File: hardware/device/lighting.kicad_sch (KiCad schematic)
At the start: 17 parts, among them U10 TRIG9, U11 TRIG13, U12 TRIG10, U13 TRIG14, U14 TRIG11, U15 TRIG15, U16 TRIG12, U17 TRIG16, U2 TRIG1, U3 TRIG2, U4 TRIG3, U5 TRIG4, U6 TRIG8, U7 TRIG7, U8 TRIG6, U9 TRIG5

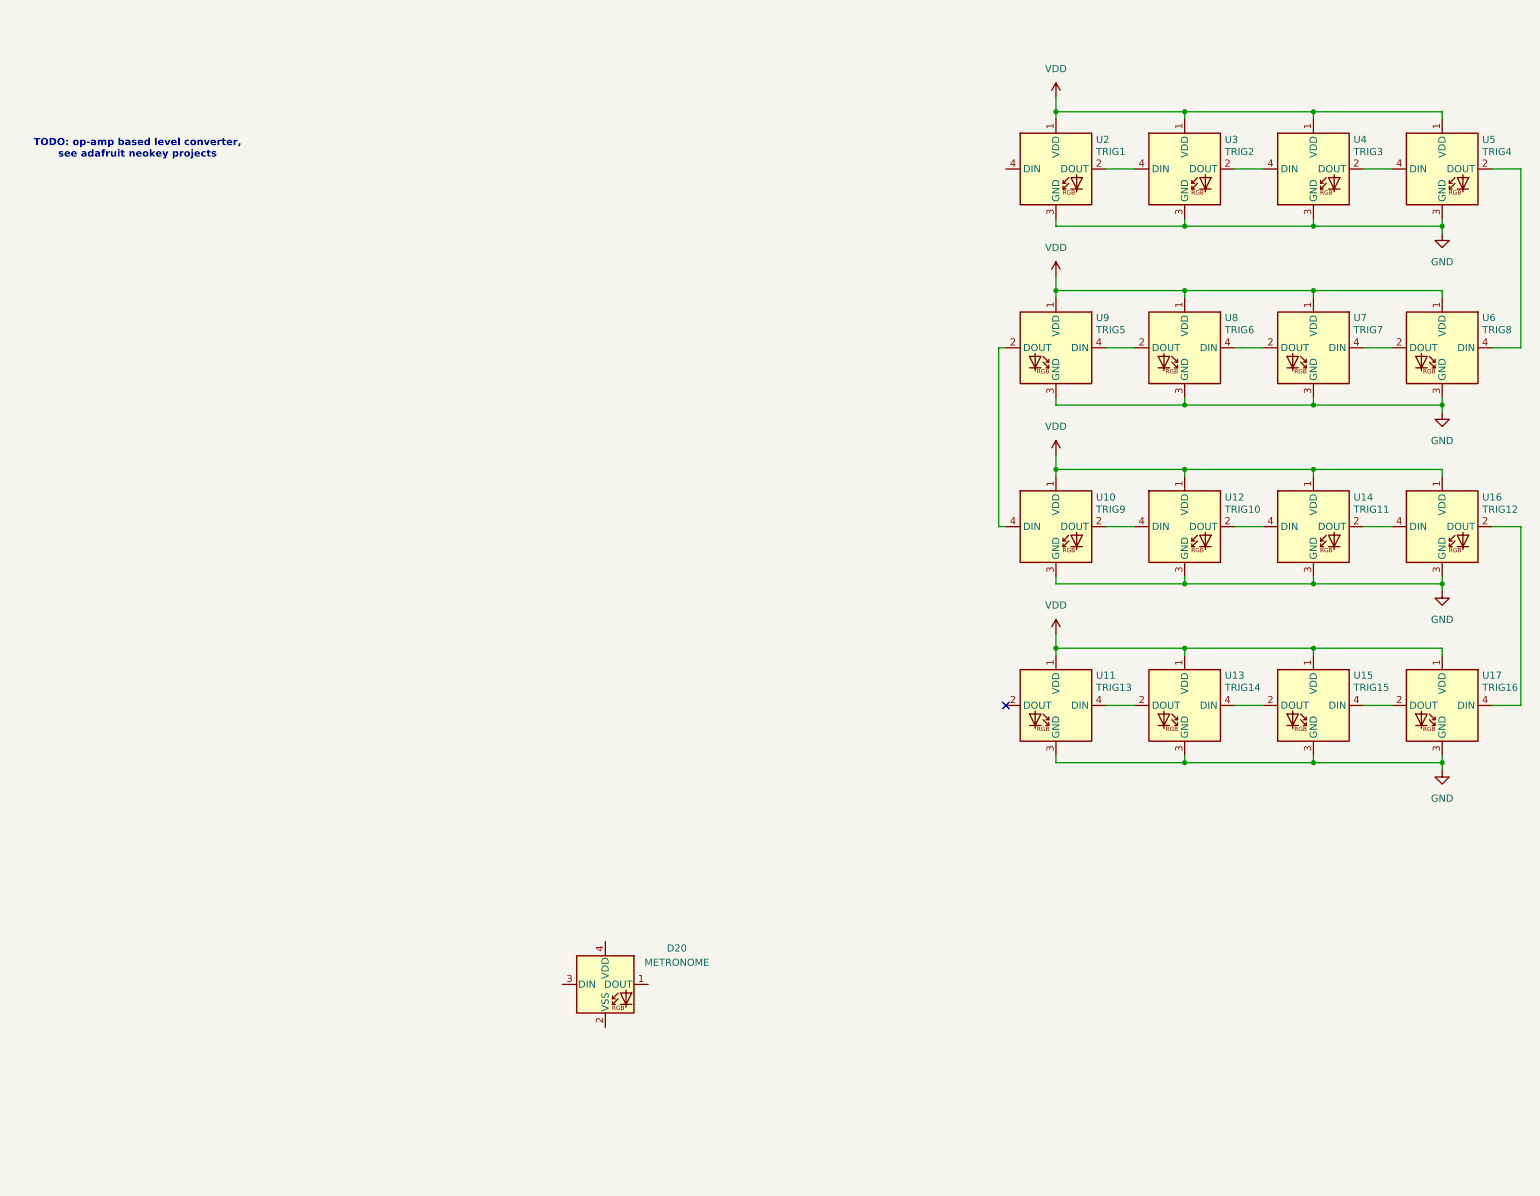
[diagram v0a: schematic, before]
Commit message: feat: add buffer for LED logic level conversion
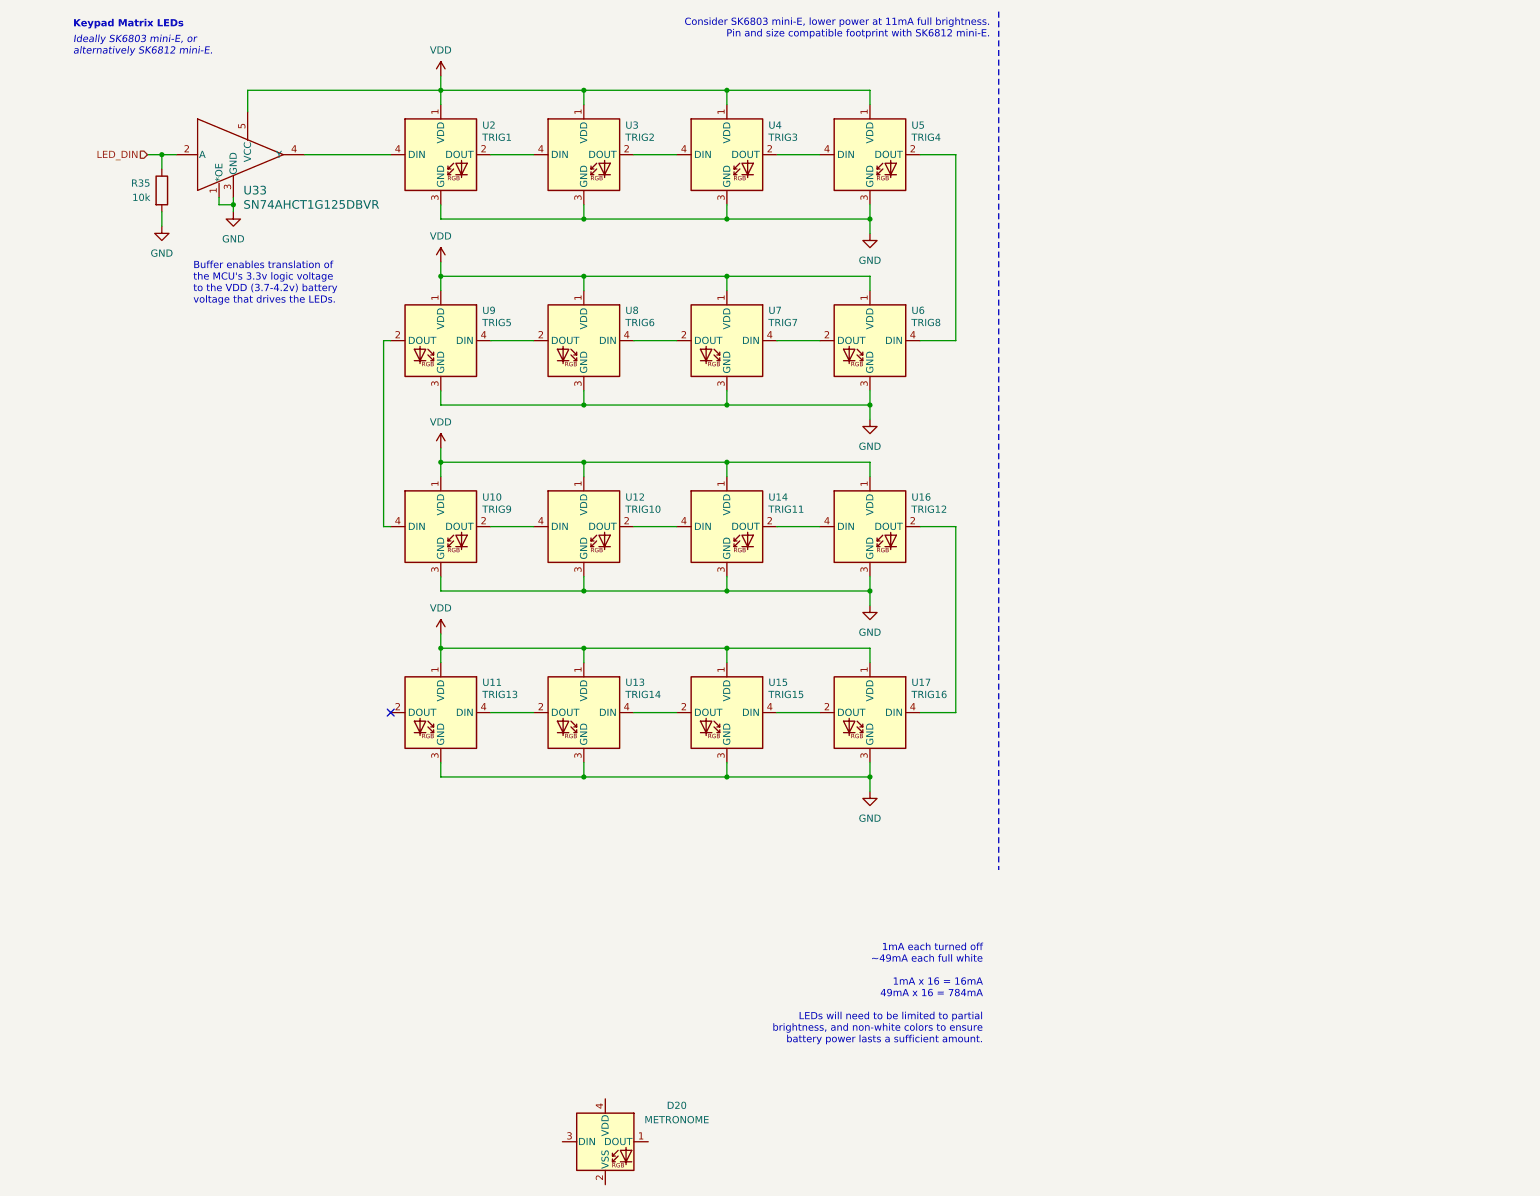
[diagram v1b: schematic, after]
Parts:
- added R35: 10k, symbol Device:R
- added U33: SN74AHCT1G125DBVR, pocket_synth:SN74AHCT1G125DBVR, symbol pocket_synth:SN74AHCT1G125DBVR
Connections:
- net GND: now also R35.2, U33.1 (*OE), U33.3 (GND)
- net VDD: now also U33.5 (VCC)
- net at U2.4 (DIN): now also U33.4 (Y)
- new net LED_DIN: R35.1, U33.2 (A)
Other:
- note added: "1mA each turned off ~49mA each full white 1mA x 16 = 16mA 49mA x 16 = 784mA LEDs will need to be limited to partial brightness, and non-white colors to ensure battery power lasts a sufficient amount."
- note added: "Buffer enables translation of the MCU's 3.3v logic voltage to the VDD (3.7-4.2v) battery voltage that drives the LEDs."
- note added: "Consider SK6803 mini-E, lower power at 11mA full brightness. Pin and size compatible footprint with SK6812 mini-E."
- note added: "Ideally SK6803 mini-E, or alternatively SK6812 mini-E."
- note added: "Keypad Matrix LEDs"
- note removed: "TODO: op-amp based level converter, see adafruit neokey projects"
- moved on the sheet: D20, U10, U11, U12, U13, U14, U15, U16, U17, U2, U3, U4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

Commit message: chore: schematic organization
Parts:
- R35: footprint (none) -> Resistor_SMD:R_0402_1005Metric
- U10, U11, U12, U13, U14, U15, U16, U17, U2, U3, U4, U5, U6, U7, U8, U9: JLC (none) -> C5149201
- U33: JLC (none) -> C7484
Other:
- moved on the sheet: D20, R35, U10, U11, U12, U13, U14, U15, U16, U17, U2, U3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
